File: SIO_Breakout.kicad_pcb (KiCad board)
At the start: 2 copper layers, 2 parts, among them J1 Atari_SIO_Connector, J2 Conn_01x13

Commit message: Layout Complete
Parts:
- J2: footprint Connector_PinHeader_2.54mm:PinHeader_1x13_P2.54mm_Horizontal -> Connector_PinHeader_2.54mm:PinHeader_1x13_P2.54mm_Vertical; moved to B.Cu
- moved J2 48.4 mm to (125.9, 101.0)
- moved J1 32.9 mm to (142.8, 111.5), turned to 180 degrees
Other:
- board outline added: 51 x 31.6 mm
- board text added: "Atari SIO Breakout Board"
- board text added: "atarimac 2026"

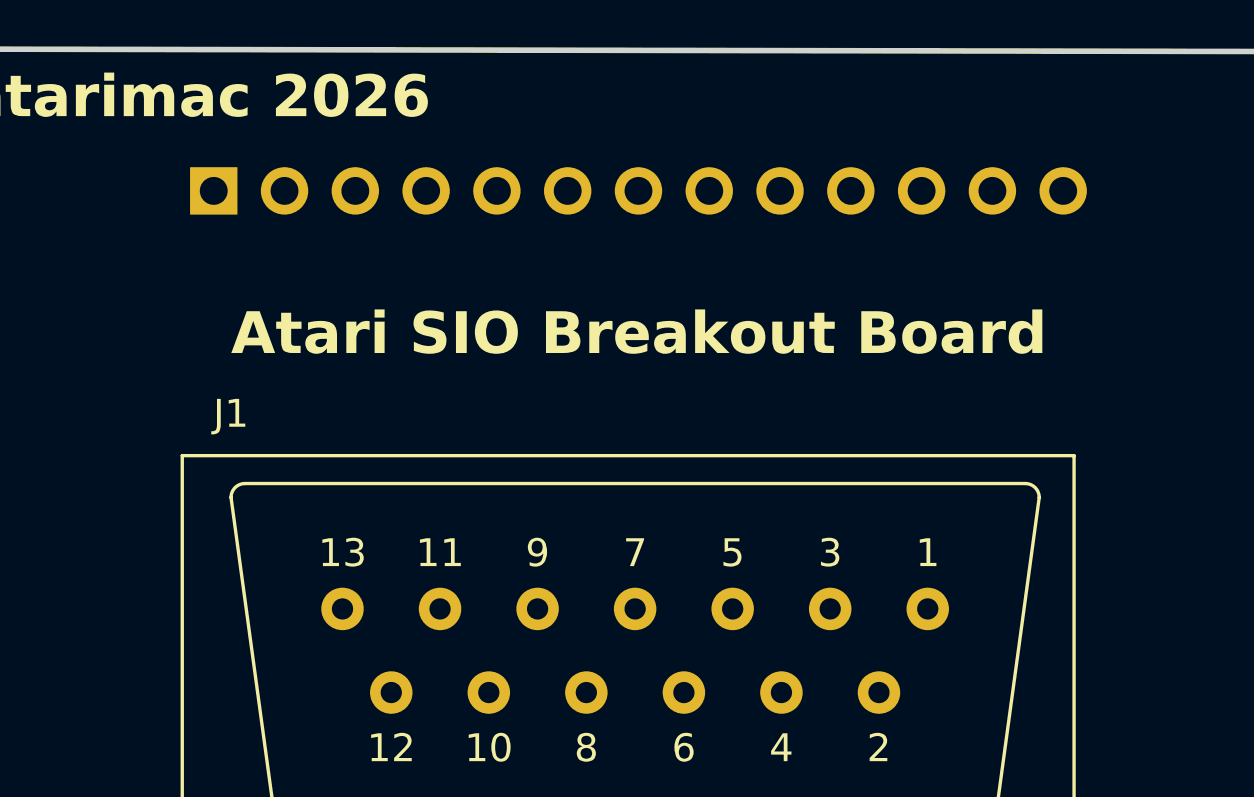
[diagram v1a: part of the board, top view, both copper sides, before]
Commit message: Flip header connector
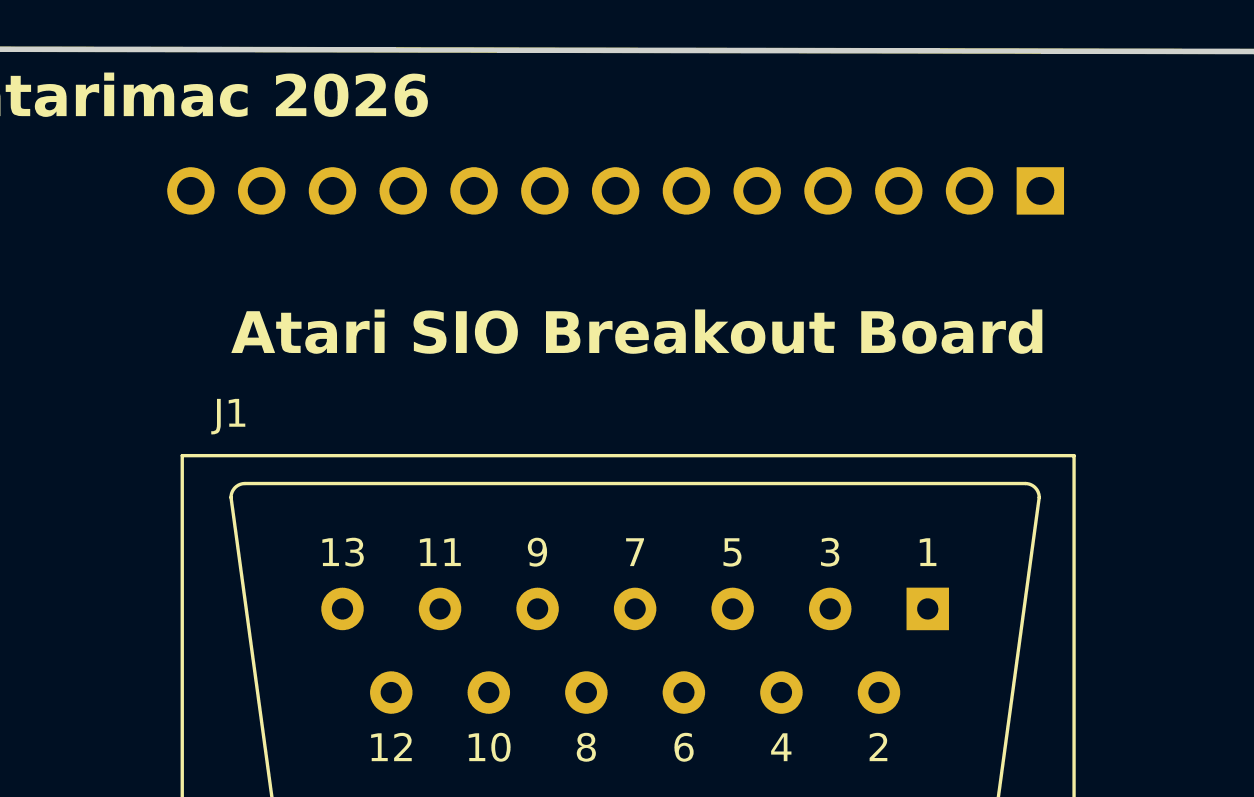
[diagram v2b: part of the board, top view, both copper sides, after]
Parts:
- moved J2 29.7 mm to (155.5, 101.0), turned to 90 degrees
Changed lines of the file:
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@@
 			)
 		)
-		(pad "1" thru_hole circle
+		(pad "1" thru_hole rect
 			(at -8.75 -4.5 180)
 			(size 1.524 1.524)
@@
 	(footprint "Connector_PinHeader_2.54mm:PinHeader_1x13_P2.54mm_Vertical"
 		(layer "B.Cu")
-		(at 125.88 101 -90)
+		(at 155.54 101 90)
 		(descr "Through hole straight pin header, 1x13, 2.54mm pitch, single row")
 		(tags "Through hole pin header THT 1x13 2.54mm single row")
@@
 		(attr through_hole)
 		(fp_line
+			(start -1.38 -31.86)
+			(end 1.38 -31.86)
+			(stroke
+				(width 0.12)
+				(type solid)
+			)
+			(layer "B.SilkS")
+		)
+		(fp_line
+			(start 1.38 -1.27)
+			(end 1.38 -31.86)
+			(stroke
+				(width 0.12)
+				(type solid)
+			)
+			(layer "B.SilkS")
+		)
+		(fp_line
+			(start -1.38 -1.27)
+			(end -1.38 -31.86)
+			(stroke
+				(width 0.12)
+				(type solid)
+			)
+			(layer "B.SilkS")
+		)
+		(fp_line
+			(start -1.38 -1.27)
+			(end 1.38 -1.27)
+			(stroke
+				(width 0.12)
+				(type solid)
+			)
+			(layer "B.SilkS")
+		)
+		(fp_line
+			(start -1.38 0)
+			(end -1.38 1.38)
+			(stroke
+				(width 0.12)
+				(type solid)
+			)
+			(layer "B.SilkS")
+		)
+		(fp_line
 			(start -1.38 1.38)
 			(end 0 1.38)
-			(stroke
-				(width 0.12)
-				(type solid)
-			)
-			(layer "B.SilkS")
-		)
-		(fp_line
-			(start -1.38 0)
-			(end -1.38 1.38)
-			(stroke
-				(width 0.12)
-				(type solid)
-			)
-			(layer "B.SilkS")
-		)
-		(fp_line
-			(start -1.38 -1.27)
-			(end 1.38 -1.27)
-			(stroke
-				(width 0.12)
-				(type solid)
-			)
-			(layer "B.SilkS")
-		)
-		(fp_line
-			(start -1.38 -1.27)
-			(end -1.38 -31.86)
-			(stroke
-				(width 0.12)
-				(type solid)
-			)
-			(layer "B.SilkS")
-		)
-		(fp_line
-			(start 1.38 -1.27)
-			(end 1.38 -31.86)
-			(stroke
-				(width 0.12)
-				(type solid)
-			)
-			(layer "B.SilkS")
-		)
-		(fp_line
-			(start -1.38 -31.86)
-			(end 1.38 -31.86)
 			(stroke
 				(width 0.12)
@@
 		)
 		(fp_line
+			(start 1.27 -31.75)
+			(end -1.27 -31.75)
+			(stroke
+				(width 0.1)
+				(type solid)
+			)
+			(layer "B.Fab")
+		)
+		(fp_line
+			(start -1.27 -31.75)
+			(end -1.27 0.635)
+			(stroke
+				(width 0.1)
+				(type solid)
+			)
+			(layer "B.Fab")
+		)
+		(fp_line
+			(start -1.27 0.635)
+			(end -0.635 1.27)
+			(stroke
+				(width 0.1)
+				(type solid)
+			)
+			(layer "B.Fab")
+		)
+		(fp_line
+			(start 1.27 1.27)
+			(end 1.27 -31.75)
+			(stroke
+				(width 0.1)
+				(type solid)
+			)
+			(layer "B.Fab")
+		)
+		(fp_line
 			(start -0.635 1.27)
 			(end 1.27 1.27)
-			(stroke
-				(width 0.1)
-				(type solid)
-			)
-			(layer "B.Fab")
-		)
-		(fp_line
-			(start 1.27 1.27)
-			(end 1.27 -31.75)
-			(stroke
-				(width 0.1)
-				(type solid)
-			)
-			(layer "B.Fab")
-		)
-		(fp_line
-			(start -1.27 0.635)
-			(end -0.635 1.27)
-			(stroke
-				(width 0.1)
-				(type solid)
-			)
-			(layer "B.Fab")
-		)
-		(fp_line
-			(start -1.27 -31.75)
-			(end -1.27 0.635)
-			(stroke
-				(width 0.1)
-				(type solid)
-			)
-			(layer "B.Fab")
-		)
-		(fp_line
-			(start 1.27 -31.75)
-			(end -1.27 -31.75)
 			(stroke
 				(width 0.1)
@@
 		)
 		(pad "1" thru_hole rect
-			(at 0 0 270)
+			(at 0 0 90)
 			(size 1.7 1.7)
 			(drill 1)
@@
 		)
 		(pad "2" thru_hole circle
-			(at 0 -2.54 270)
+			(at 0 -2.54 90)
 			(size 1.7 1.7)
 			(drill 1)
@@
 		)
 		(pad "3" thru_hole circle
-			(at 0 -5.08 270)
+			(at 0 -5.08 90)
 			(size 1.7 1.7)
 			(drill 1)
@@
 		)
 		(pad "4" thru_hole circle
-			(at 0 -7.62 270)
+			(at 0 -7.62 90)
 			(size 1.7 1.7)
 			(drill 1)
@@
 		)
 		(pad "5" thru_hole circle
-			(at 0 -10.16 270)
+			(at 0 -10.16 90)
 			(size 1.7 1.7)
 			(drill 1)
@@
 		)
 		(pad "6" thru_hole circle
-			(at 0 -12.7 270)
+			(at 0 -12.7 90)
 			(size 1.7 1.7)
 			(drill 1)
@@
 		)
 		(pad "7" thru_hole circle
-			(at 0 -15.24 270)
+			(at 0 -15.24 90)
 			(size 1.7 1.7)
 			(drill 1)
@@
 		)
 		(pad "8" thru_hole circle
-			(at 0 -17.78 270)
+			(at 0 -17.78 90)
 			(size 1.7 1.7)
 			(drill 1)
@@
 		)
 		(pad "9" thru_hole circle
-			(at 0 -20.32 270)
+			(at 0 -20.32 90)
 			(size 1.7 1.7)
 			(drill 1)
@@
 		)
 		(pad "10" thru_hole circle
-			(at 0 -22.86 270)
+			(at 0 -22.86 90)
 			(size 1.7 1.7)
 			(drill 1)
@@
 		)
 		(pad "11" thru_hole circle
-			(at 0 -25.4 270)
+			(at 0 -25.4 90)
 			(size 1.7 1.7)
 			(drill 1)
@@
 		)
 		(pad "12" thru_hole circle
-			(at 0 -27.94 270)
+			(at 0 -27.94 90)
 			(size 1.7 1.7)
 			(drill 1)
@@
 		)
 		(pad "13" thru_hole circle
-			(at 0 -30.48 270)
-			(size 1.7 1.7)
-			(drill 1)
+			(at 0 -30.48 90)
+			(size 1.7 1.7)
+			(drill 1)

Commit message: Initial Routing
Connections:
- J1 pad 1: unconnected-(J1-Clock_Input-Pad1) -> Net-(J1-Clock_Input)
- J1 pad 10: unconnected-(J1-+5V/Ready-Pad10) -> Net-(J1-+5V/Ready)
- J1 pad 11: unconnected-(J1-Audio_Input-Pad11) -> Net-(J1-Audio_Input)
- J1 pad 12: unconnected-(J1-+12V-Pad12) -> Net-(J1-+12V)
- J1 pad 13: unconnected-(J1-Interrupt-Pad13) -> Net-(J1-Interrupt)
- J1 pad 2: unconnected-(J1-Clock_Output-Pad2) -> Net-(J1-Clock_Output)
- J1 pad 3: unconnected-(J1-Data_Input-Pad3) -> Net-(J1-Data_Input)
- J1 pad 4: unconnected-(J1-Ground-Pad4) -> Net-(J2-Pin_4)
- J1 pad 5: unconnected-(J1-Data_Output-Pad5) -> Net-(J1-Data_Output)
- J1 pad 6: unconnected-(J1-Ground-Pad6) -> Net-(J2-Pin_6)
- J1 pad 7: unconnected-(J1-Command-Pad7) -> Net-(J1-Command)
- J1 pad 8: unconnected-(J1-Motor_Control-Pad8) -> Net-(J1-Motor_Control)
- J1 pad 9: unconnected-(J1-Proceed-Pad9) -> Net-(J1-Proceed)
- J2 pad 1: unconnected-(J2-Pin_1-Pad1) -> Net-(J1-Clock_Input)
- J2 pad 10: unconnected-(J2-Pin_10-Pad10) -> Net-(J1-+5V/Ready)
- J2 pad 11: unconnected-(J2-Pin_11-Pad11) -> Net-(J1-Audio_Input)
- J2 pad 12: unconnected-(J2-Pin_12-Pad12) -> Net-(J1-+12V)
- J2 pad 13: unconnected-(J2-Pin_13-Pad13) -> Net-(J1-Interrupt)
- J2 pad 2: unconnected-(J2-Pin_2-Pad2) -> Net-(J1-Clock_Output)
- J2 pad 3: unconnected-(J2-Pin_3-Pad3) -> Net-(J1-Data_Input)
- J2 pad 4: unconnected-(J2-Pin_4-Pad4) -> Net-(J2-Pin_4)
- J2 pad 5: unconnected-(J2-Pin_5-Pad5) -> Net-(J1-Data_Output)
- J2 pad 6: unconnected-(J2-Pin_6-Pad6) -> Net-(J2-Pin_6)
- J2 pad 7: unconnected-(J2-Pin_7-Pad7) -> Net-(J1-Command)
- J2 pad 8: unconnected-(J2-Pin_8-Pad8) -> Net-(J1-Motor_Control)
- J2 pad 9: unconnected-(J2-Pin_9-Pad9) -> Net-(J1-Proceed)
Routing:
- net Net-(J1-+12V): track 0.00 -> 19.9 mm
- net Net-(J1-Clock_Output): track 0.00 -> 19.3 mm
- net Net-(J1-+5V/Ready): track 0.00 -> 19.3 mm
- net Net-(J2-Pin_4): track 0.00 -> 18.7 mm
- net Net-(J1-Motor_Control): track 0.00 -> 18.6 mm
- net Net-(J2-Pin_6): track 0.00 -> 18.0 mm
- net Net-(J1-Interrupt): track 0.00 -> 17.3 mm
- net Net-(J1-Clock_Input): track 0.00 -> 16.7 mm
- net Net-(J1-Audio_Input): track 0.00 -> 16.6 mm
- net Net-(J1-Data_Input): track 0.00 -> 16.0 mm
- net Net-(J1-Proceed): track 0.00 -> 15.9 mm
- net Net-(J1-Data_Output): track 0.00 -> 15.4 mm
- net Net-(J1-Command): track 0.00 -> 15.3 mm
